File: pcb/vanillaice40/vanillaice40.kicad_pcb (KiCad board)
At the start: 2 copper layers, 100 x 62 mm, 105 parts, among them J1 FX18-120S-0.8SV20, J2 SM04B-SRSS-TBLFSN, J3 SM04B-SRSS-TBLFSN, SW1 USR1, SW2 USR1, SW3 RESET, U1 TPS563252DRLR, U2 ICE40HX4K-TQ144, U3 W25X40CLSN, U4 TPS563252DRLR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

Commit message: rough pcb placement done
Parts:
- removed J3: SM04B-SRSS-TBLFSN, SM04B-SRSS-TB-LF-SN:CONN_SM04B_JST
- added D6: Red, Diode_SMD:D_0603_1608Metric, F.Cu at (82.4, 35.3)
- added D7: Red, Diode_SMD:D_0603_1608Metric, F.Cu at (79.1, 35.3)
- added R38: 2.2k, Resistor_SMD:R_0603_1608Metric, F.Cu at (82.4, 38.9)
- added R39: 2.2k, Resistor_SMD:R_0603_1608Metric, F.Cu at (79.1, 38.9)
- D4: value Green -> Red
- R24, R25, R26, R27, R28, R29, R32, R33, R6: moved to B.Cu
- moved C41 257.7 mm to (50.9, 80.8), turned to 180 degrees
- moved C42 254.4 mm to (63.9, 71.8)
- moved C37 250.2 mm to (66.4, 61.3), turned to 180 degrees
- moved C43 248.0 mm to (63.9, 66.3), turned to 180 degrees
- moved C39 243.4 mm to (78.2, 53.1), turned to 90 degrees
- moved FB2 239.5 mm to (75.3, 74.3), turned to 180 degrees
- moved R31 239.3 mm to (83.9, 73.5), turned to 90 degrees
- moved R27 238.6 mm to (93.3, 72.2)
- moved C21 236.0 mm to (75.3, 72.1), turned to 0 degrees
- moved R24 235.0 mm to (93.3, 81.5)
- moved FB3 235.0 mm to (71.6, 74.2), turned to 0 degrees
- moved R28 233.4 mm to (93.3, 69.0)
- moved C36 232.4 mm to (82.7, 63.8), turned to 0 degrees
- moved C22 232.1 mm to (75.3, 69.7), turned to 0 degrees
- moved C32 231.7 mm to (71.6, 72.1), turned to 180 degrees
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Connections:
- R6 pad 1: Net-(X1-OUT) -> Net-(X1-OE)
- R6 pad 2: /IOL_14A -> +3V3
- X1 pad 1: +3V3 -> Net-(X1-OE)
- X1 pad 3: Net-(X1-OUT) -> /IOL_14A

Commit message: drc constraints
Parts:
- added J3: Conn_01x02_Pin, Connector_PinHeader_2.54mm:PinHeader_1x02_P2.54mm_Vertical, F.Cu at (43.8, 45.2)
- C13, C14, C15, C16, C19, C20, C23, FB1, L1, L2, R10, R11, R13, R14, R17, R21, R22, R23, R9, U1, U4: moved to B.Cu
- moved C16 13.8 mm to (59.6, 51.7)
- moved C23 13.0 mm to (59.2, 65.1)
- moved R22 8.33 mm to (48.6, 61.1), turned to 180 degrees
- moved R23 8.33 mm to (48.6, 58.3), turned to 180 degrees
- moved C19 7.92 mm to (56.7, 59.6)
- moved C14 7.67 mm to (56.6, 47.2)
- moved L1 7.67 mm to (56.6, 50.5), turned to 0 degrees
- moved R14 7.44 mm to (49.0, 45.9), turned to 180 degrees
- moved R17 7.44 mm to (49.0, 47.4), turned to 0 degrees
- moved L2 6.91 mm to (56.2, 63.1), turned to 0 degrees
- moved R21 6.81 mm to (49.3, 64.6)
- moved R11 3.51 mm to (51.0, 52.1)
- moved D5 3.44 mm to (91.8, 34.9)
- moved R12 3.44 mm to (91.8, 38.6)
- moved R38 3.44 mm to (85.9, 38.6)
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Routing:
- added copper zone on In2.Cu, net +3V3
- added copper zone on In1.Cu, net GND
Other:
- copper layers 2 -> 4

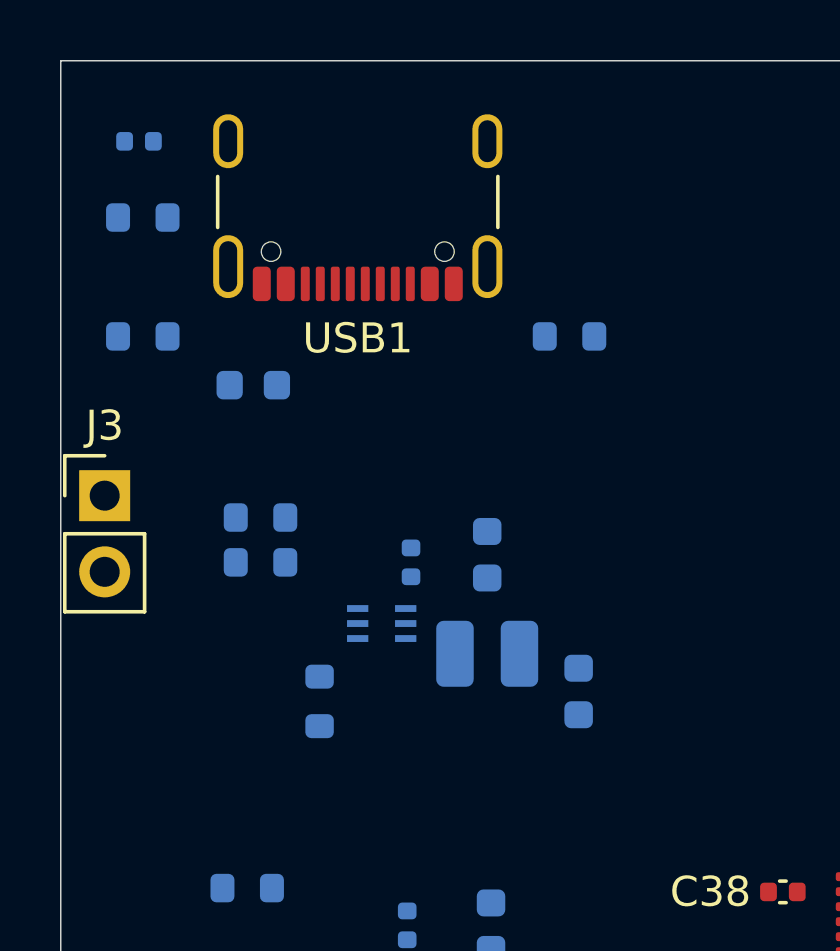
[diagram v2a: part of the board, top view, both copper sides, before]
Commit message: usb power routing
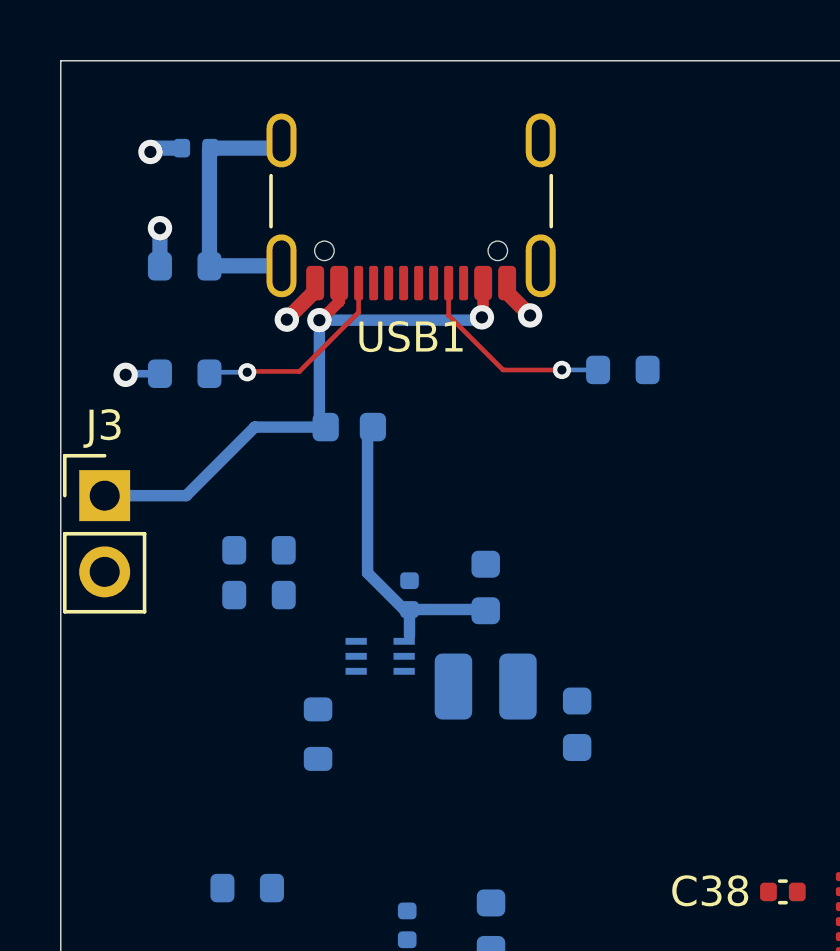
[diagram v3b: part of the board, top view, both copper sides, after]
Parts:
- moved FB1 3.49 mm to (52.0, 42.9), turned to 0 degrees
- moved R13 2.14 mm to (46.5, 37.6)
- moved R10 2.10 mm to (61.1, 41.0), turned to 180 degrees
- moved C13 1.92 mm to (46.9, 33.6)
- moved R9 1.87 mm to (46.5, 41.1)
- moved USB1 1.78 mm to (54.0, 34.4)
- moved C14 1.09 mm to (56.5, 48.3)
- moved L1 1.09 mm to (56.5, 51.6)
- moved R11 1.09 mm to (50.9, 53.2)
- moved R14 1.09 mm to (49.0, 47.0)
- moved R17 1.09 mm to (49.0, 48.5)
- moved C15 1.09 mm to (54.0, 48.5)
- moved C16 1.09 mm to (59.6, 52.8)
- moved U1 1.09 mm to (53.0, 50.6)
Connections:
- net Net-(J3-Pin_1) renamed /U5V
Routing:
- net /U5V: track 0.00 -> 20.1 mm, vias 0 -> 2
- net VBUS_5V: track 0.00 -> 10.3 mm
- net Net-(USB1-SHIELD): track 0.00 -> 9.04 mm
- net Net-(USB1-CC1): track 0.00 -> 6.81 mm, vias 0 -> 1
- net Net-(USB1-CC2): track 0.00 -> 6.79 mm, vias 0 -> 1
- net GND: track 0.00 -> 6.73 mm, vias 0 -> 5

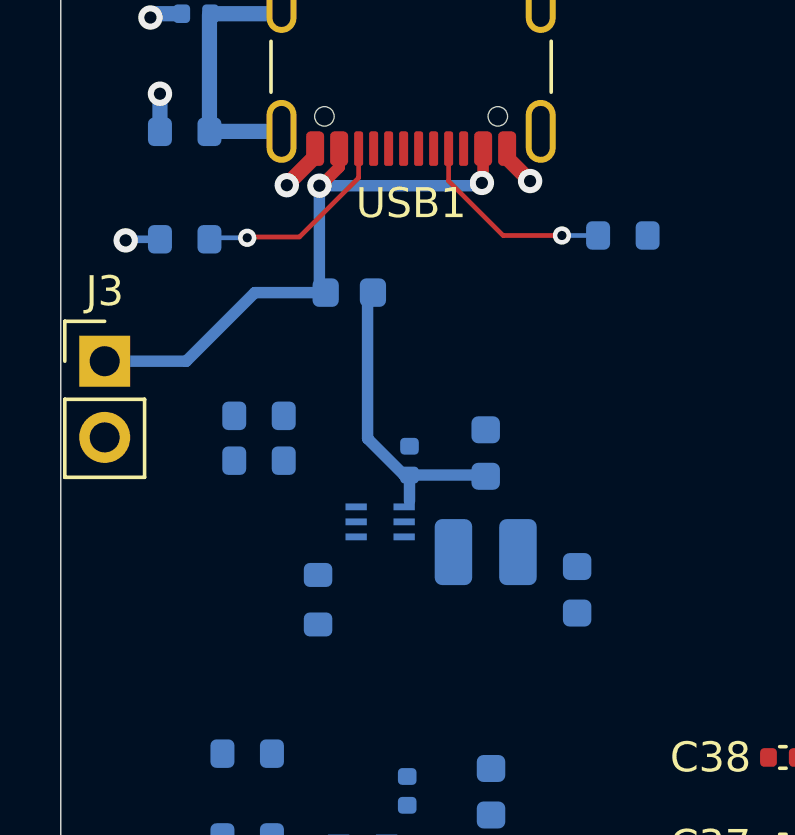
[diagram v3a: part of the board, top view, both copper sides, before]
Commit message: 3v3 regulator layout
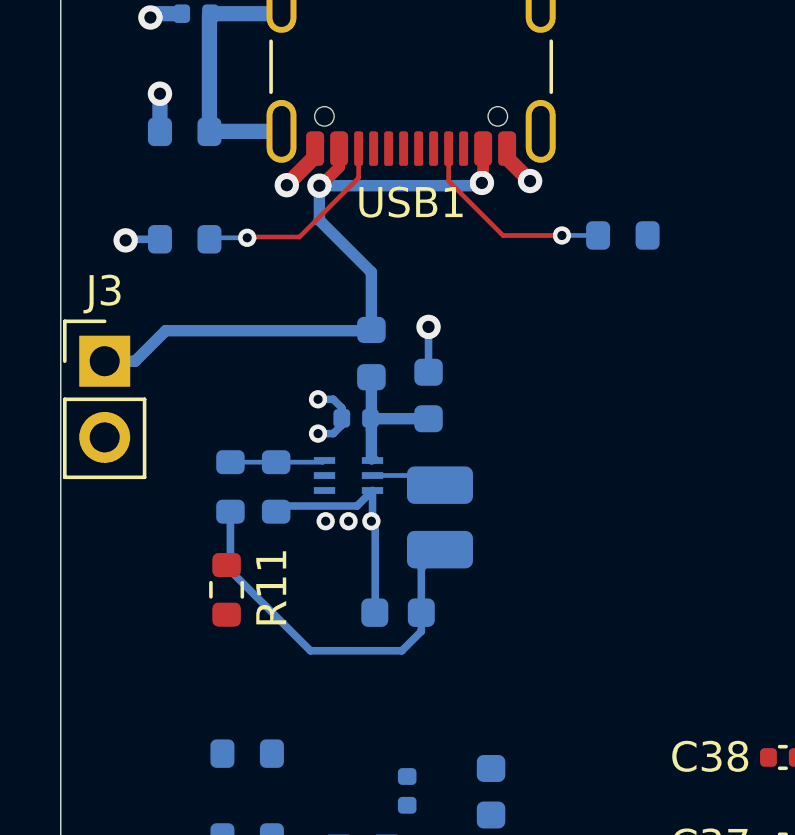
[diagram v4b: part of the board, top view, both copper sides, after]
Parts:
- R11: moved to F.Cu
- moved C16 6.02 mm to (53.6, 53.6), turned to 180 degrees
- moved R11 3.07 mm to (47.9, 52.8)
- moved C14 2.70 mm to (54.6, 46.4)
- moved R14 2.55 mm to (48.0, 49.4), turned to -90 degrees
- moved C15 2.27 mm to (52.2, 47.1), turned to 180 degrees
- moved FB1 2.16 mm to (52.7, 45.0), turned to -90 degrees
- moved L1 1.91 mm to (55.0, 50.4), turned to -90 degrees
- moved U1 1.87 mm to (51.9, 49.0)
- moved R17 1.05 mm to (49.5, 49.4), turned to 90 degrees
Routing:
- net +3V3: track 0.00 -> 12.7 mm
- net GND: track 6.73 -> 18.3 mm, vias 5 -> 11
- net VBUS_5V: track 10.3 -> 4.34 mm
- net Net-(U1-FB): track 0.00 -> 3.16 mm
- net /U5V: track 20.1 -> 23.0 mm
- net Net-(U1-SW): track 0.00 -> 2.19 mm

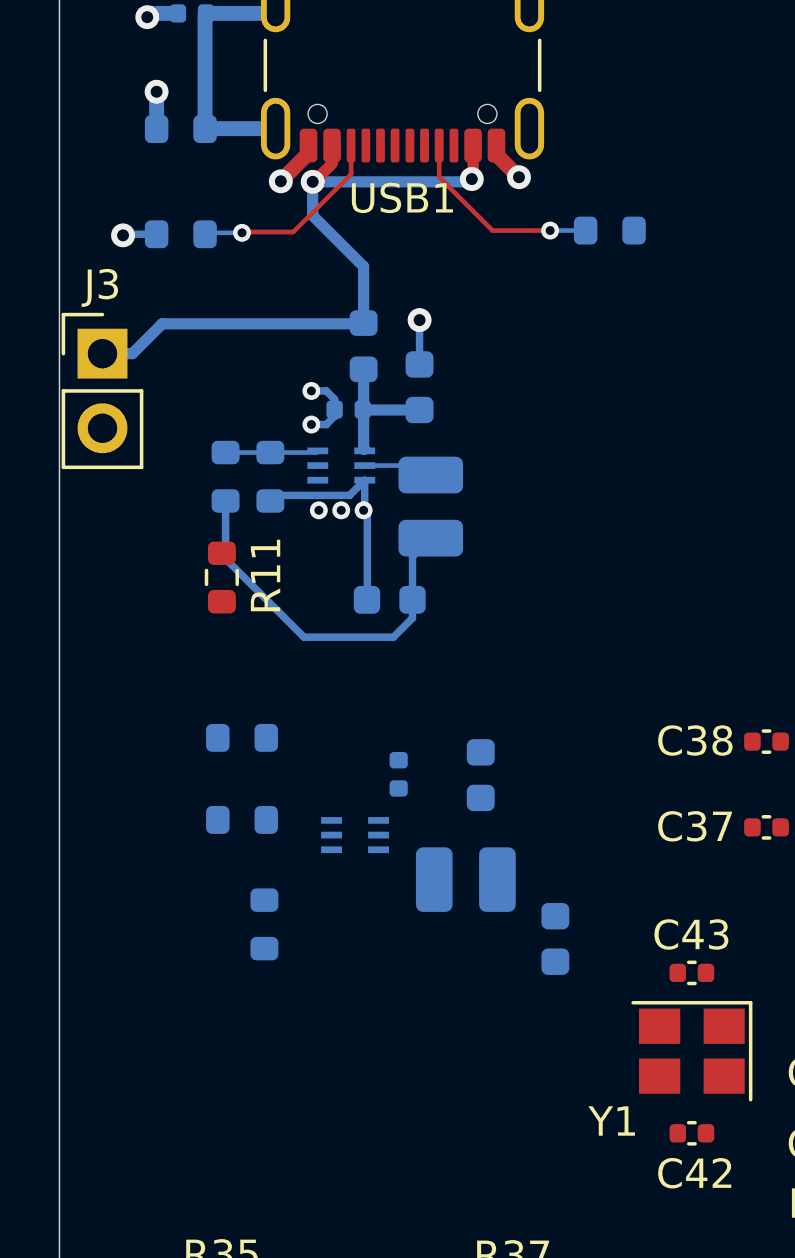
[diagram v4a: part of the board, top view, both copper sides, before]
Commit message: 1v2 regulator
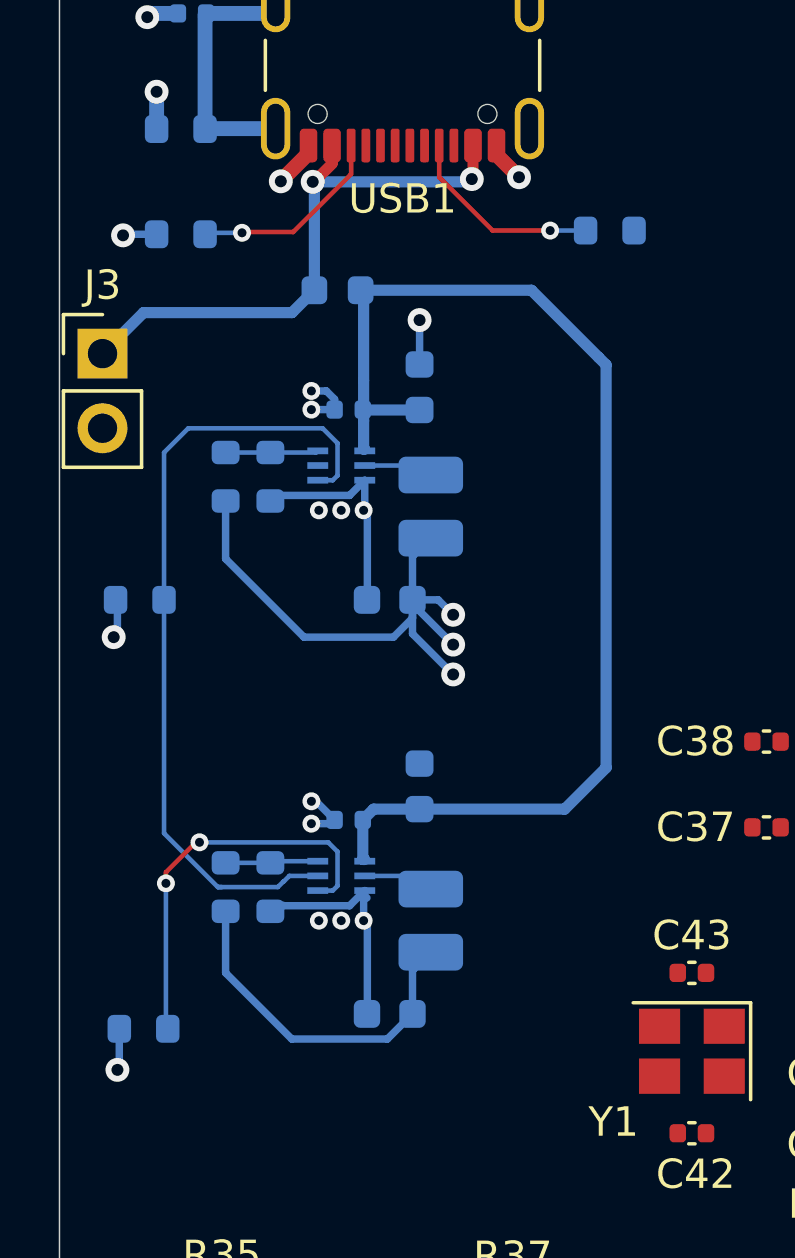
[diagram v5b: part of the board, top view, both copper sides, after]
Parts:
- R11: moved to B.Cu
- moved C23 6.19 mm to (53.6, 67.7), turned to 180 degrees
- moved R21 5.44 mm to (45.2, 68.2), turned to 0 degrees
- moved R23 5.17 mm to (49.5, 63.4), turned to 90 degrees
- moved R11 2.90 mm to (45.1, 53.6), turned to 0 degrees
- moved R22 2.35 mm to (48.0, 63.4), turned to -90 degrees
- moved C20 2.30 mm to (52.2, 61.1), turned to 180 degrees
- moved C19 2.12 mm to (54.6, 59.9)
- moved FB1 2.10 mm to (51.8, 43.1), turned to 0 degrees
- moved L2 1.84 mm to (55.0, 64.5), turned to -90 degrees
- moved U4 1.47 mm to (51.9, 63.0)
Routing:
- net VBUS_5V: track 4.34 -> 40.6 mm
- net Net-(U1-PG): track 0.00 -> 27.5 mm
- net +1V2: track 0.00 -> 13.5 mm, vias 0 -> 1
- net Net-(U4-PG): track 0.00 -> 13.4 mm, vias 0 -> 2
- net GND: track 18.3 -> 27.2 mm, vias 11 -> 16
- net +3V3: track 12.7 -> 20.9 mm, vias 0 -> 4
- net Net-(U4-FB): track 0.00 -> 3.16 mm
- net /U5V: track 23.0 -> 20.0 mm
- net Net-(U4-SW): track 0.00 -> 2.49 mm

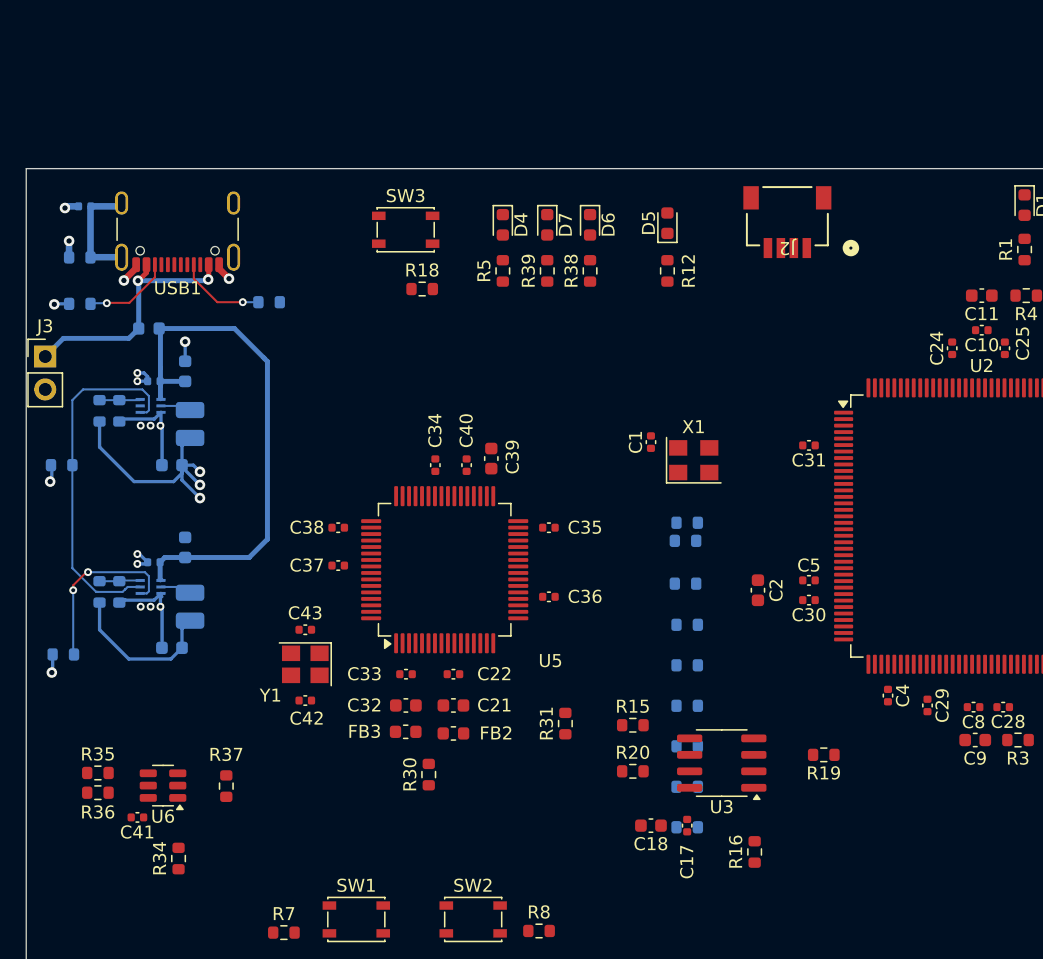
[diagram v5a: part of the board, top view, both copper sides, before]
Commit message: FT2232HL - clock and eeprom routing
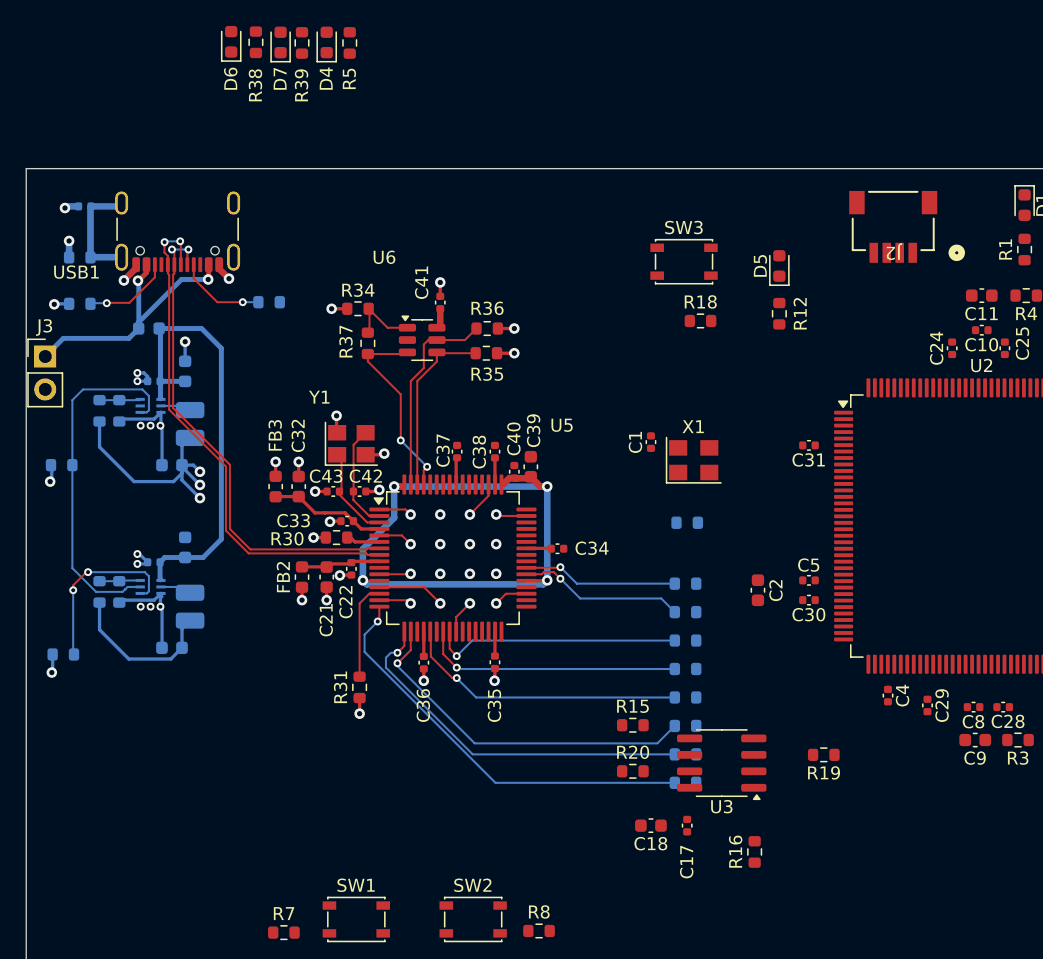
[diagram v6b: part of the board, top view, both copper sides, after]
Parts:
- moved R36 46.7 mm to (77.9, 43.1), turned to 180 degrees
- moved C41 46.1 mm to (74.3, 41.0), turned to 90 degrees
- moved R34 44.6 mm to (67.9, 41.5), turned to 0 degrees
- moved R35 44.1 mm to (77.9, 45.0), turned to 180 degrees
- moved U6 39.8 mm to (72.9, 43.9), turned to 0 degrees
- moved R37 35.9 mm to (68.7, 44.2), turned to -90 degrees
- moved R38 31.2 mm to (60.1, 21.0)
- moved D6 31.1 mm to (58.2, 20.9), turned to 90 degrees
- moved R39 25.8 mm to (63.6, 21.0)
- moved D7 24.9 mm to (62.0, 21.0), turned to 90 degrees
- moved R18 21.6 mm to (94.4, 42.5)
- moved SW3 21.6 mm to (93.1, 37.9)
- moved FB3 21.4 mm to (61.6, 55.2), turned to -90 degrees
- moved R5 21.2 mm to (67.3, 21.0)
- moved R30 19.6 mm to (66.3, 59.2), turned to 0 degrees
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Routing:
- net /FT_VCORE: track 0.00 -> 49.6 mm, vias 0 -> 4
- net /USB_DP: track 0.00 -> 40.0 mm, vias 0 -> 2
- net GND: track 27.2 -> 65.6 mm, vias 16 -> 44
- net /USB_DN: track 0.00 -> 38.2 mm, vias 0 -> 2
- net Net-(U5-ADBUS0): track 0.00 -> 32.1 mm, vias 0 -> 1
- net Net-(U5-ADBUS1): track 0.00 -> 28.7 mm, vias 0 -> 1
- net Net-(U5-ADBUS2): track 0.00 -> 27.5 mm, vias 0 -> 1
- net Net-(U5-ADBUS4): track 0.00 -> 22.1 mm, vias 0 -> 1
- net Net-(U5-ADBUS6): track 0.00 -> 20.1 mm, vias 0 -> 1
- net Net-(U5-ADBUS7): track 0.00 -> 19.4 mm, vias 0 -> 1
- net +3V3: track 20.9 -> 39.8 mm, vias 4 -> 10
- net Net-(U5-EECS): track 0.00 -> 15.8 mm
- net Net-(U5-EEDATA): track 0.00 -> 15.2 mm, vias 0 -> 2
- net Net-(U5-EECLK): track 0.00 -> 13.8 mm
- net Net-(U5-BDBUS0): track 0.00 -> 12.8 mm, vias 0 -> 1
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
